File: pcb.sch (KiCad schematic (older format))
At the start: 1 part, among them U3 LC709203FQH-01TWG

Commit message: Did stuff
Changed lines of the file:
@@
 $EndComp
 $Sheet
-S 5950 3275 725  1050
+S 5075 3275 725  1050
 U 5F797DCE
 F0 "Power" 50
 F1 "power.sch" 50
-F2 "SDA" B L 5950 3500 50
-F3 "SCL" I L 5950 3575 50
-F4 "3v3" O L 5950 3350 50
+F2 "SDA" B R 5800 3500 50
+F3 "SCL" I R 5800 3575 50
+F4 "3v3" O R 5800 3350 50
 $EndSheet
 Wire Wire Line
@@
 	5875 3350 5875 3275
 $Comp
-L power:+3V3 #PWR?
+L power:+3V3 #PWR0101
 U 1 1 5FCAFF6A
 P 5875 3275
-F 0 "#PWR?" H 5875 3125 50  0001 C CNN
+F 0 "#PWR0101" H 5875 3125 50  0001 C CNN
 F 1 "+3V3" H 5890 3448 50  0000 C CNN
 F 2 "" H 5875 3275 50  0001 C CNN
@@
 	5800 3575 5950 3575
 $Sheet
-S 5075 3275 725  1050
+S 5950 3275 725  1050
 U 5FCCBFB4
 F0 "MCU + I/O" 50
 F1 "MCU+IO.sch" 50
-F2 "SCL" O R 5800 3575 50
-F3 "SDA" B R 5800 3500 50
-F4 "3V3" B R 5800 3350 50
+F2 "SCL" O L 5950 3575 50
+F3 "SDA" B L 5950 3500 50
+F4 "3V3" B L 5950 3350 50
 $EndSheet
 Text Notes 3200 6100 0    50   ~ 0

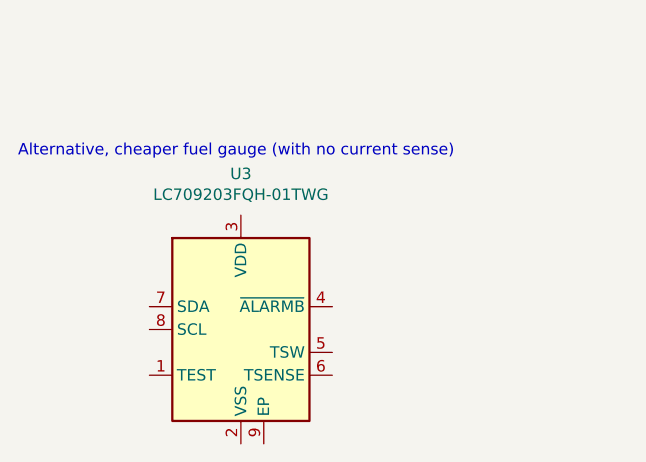
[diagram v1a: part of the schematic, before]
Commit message: Added alternative fuel gauge to PCB
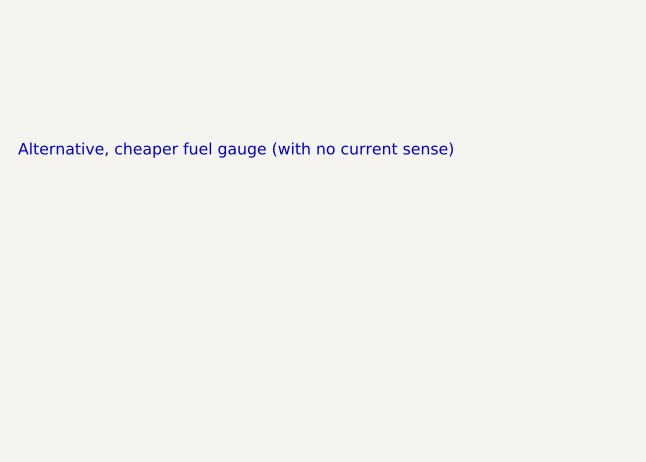
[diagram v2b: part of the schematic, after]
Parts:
- removed U3: LC709203FQH-01TWG, Package_DFN_QFN:WDFN-8-1EP_4x3mm_P0.65mm_EP2.4x1.8mm, symbol Battery_Management:LC709203FQH-01TWG
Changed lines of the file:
@@
 Comment4 "WiFi connected IR blaster / reciever"
 $EndDescr
-$Comp
-L Battery_Management:LC709203FQH-01TWG U3
-U 1 1 5F5106E8
-P 4175 6850
-F 0 "U3" H 4175 7531 50  0000 C CNN
-F 1 "LC709203FQH-01TWG" H 4175 7440 50  0000 C CNN
-F 2 "Package_DFN_QFN:WDFN-8-1EP_4x3mm_P0.65mm_EP2.4x1.8mm" H 4175 6300 50  0001 C CNN
-F 3 "https://www.onsemi.com/pub/Collateral/LC709203F-D.PDF" H 4125 6750 50  0001 C CNN
-	1    4175 6850
-	1    0    0    -1
-$EndComp
 $Sheet
 S 5075 3275 725  1050

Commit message: Added stuff
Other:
- note removed: "Alternative, cheaper fuel gauge (with no current sense)"
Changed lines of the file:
@@
 F4 "3V3" B L 5950 3350 50
 $EndSheet
-Text Notes 3200 6100 0    50   ~ 0
-Alternative, cheaper fuel gauge (with no current sense)
 $EndSCHEMATC
